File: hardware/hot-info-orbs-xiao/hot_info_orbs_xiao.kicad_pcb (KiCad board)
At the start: 2 copper layers, 198.8 x 28.5 mm, 13 parts, among them SW1 SW_Push, SW2 SW_Push, SW3 SW_Push, U2 XIAO ESP32-S3 Plus

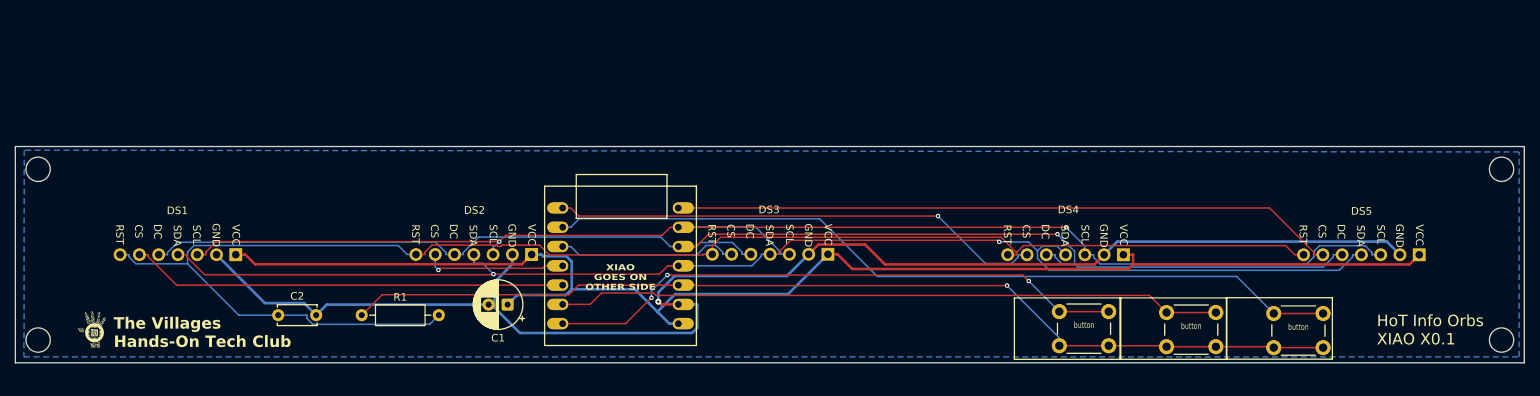
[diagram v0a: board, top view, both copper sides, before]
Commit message: xiao: physical rework, placed not routed (sockets, top-edge switches, no antenna patch)
Scott 2026-10-16: no antenna on the board, displays as low as possible on
headers into female sockets, right-angle 6x6x8 switches on the TOP edge
equally spaced in the centre third, C1/C2/R1 to the bottom. Physicals
first, route after he checks the STEP - so all tracks are stripped and the
pour is unfilled; DRC shows 46 unconnected and 0 parity on purpose.

- ANTENNA_PATCH and its silk removed; antenna_patch.py retired.
- DS1-5 -> new _Displays:GC9A01_SOCKET (same pads, PinSocket_1x07 model,
  display lifted 8.5 mm), pad row y 106.01 = the 0.5 mm edge rule + margin.
- SW1-3 -> stock PTS645Vx39 right-angle. Rejected the other PTS645 angled
  variants: Vx39's 8.05 mm overall depth is the one nearest "6x6x8". Its
  7.0 mm tab pitch vs the listing's 6.5 mm is unverified - measure a part.
- R1 in the DS1/DS2 gap, C1+C2 in DS3/DS4. Rejected the DS2/DS3 gap: the
  XIAO is on the back there and THT leads would hit it.
- Every Remove deferred to the end: after the first b.Remove() SWIG stops
  typing every return value, not just Zones() as HANDOFF had it.

Co-Authored-By: Claude Opus 5.5 <noreply@anthropic.com>
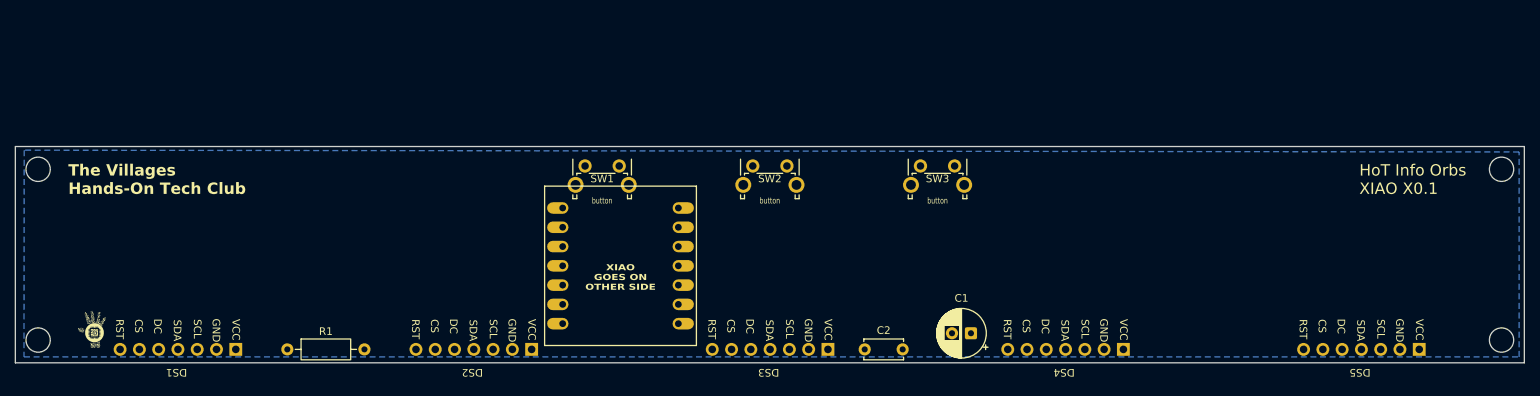
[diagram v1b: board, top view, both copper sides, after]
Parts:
- DS1, DS2, DS3, DS4, DS5: footprint _Displays:GC9A01_PINS -> _Displays:GC9A01_SOCKET
- SW1, SW2, SW3: footprint Button_Switch_THT:SW_PUSH_6mm_H5mm -> Button_Switch_THT:SW_Tactile_SPST_Angled_PTS645Vx39-2LFS
- moved C2 77.4 mm to (163.3, 106.0)
- moved SW1 65.4 mm to (126.4, 81.8)
- moved C1 61.2 mm to (177.3, 103.9)
- moved SW2 57.8 mm to (148.5, 81.8)
- moved SW3 50.4 mm to (170.6, 81.8)
- moved DS3 12.5 mm to (149.0, 102.5)
- moved DS2 12.5 mm to (110.0, 102.5)
- moved DS1 12.5 mm to (71.0, 102.5)
- moved DS4 12.5 mm to (188.0, 102.5)
- moved DS5 12.5 mm to (226.9, 102.5)
- moved R1 10.8 mm to (87.2, 106.0)
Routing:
- net /RST: track 202.3 -> 0.00 mm
- net GND: track 189.8 -> 0.00 mm, vias 1 -> 0
- net +5V: track 182.2 -> 0.00 mm
- net /SCLK: track 181.1 -> 0.00 mm, vias 2 -> 0
- net /DC: track 178.5 -> 0.00 mm, vias 1 -> 0
- net /MOSI: track 171.4 -> 0.00 mm, vias 2 -> 0
- net /3V3: track 132.3 -> 0.00 mm, vias 1 -> 0
- net /SW3: track 105.8 -> 0.00 mm
- net /SW2: track 87.8 -> 0.00 mm
- net /CS5: track 87.6 -> 0.00 mm
- net /SW1: track 77.1 -> 0.00 mm, vias 3 -> 0
- net /CS4: track 64.9 -> 0.00 mm, vias 1 -> 0
- net /CS1: track 57.6 -> 0.00 mm
- net /CS3: track 23.9 -> 0.00 mm
- net /CS2: track 18.8 -> 0.00 mm, vias 1 -> 0
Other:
- board text removed: "STICK FPC ANTENNA HERE no copper under this box"

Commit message: xiao: passives and switches to the XIAO's side, top edge up to the display tops
Scott 2026-10-16: "bottom of the board" meant the side, not the edge - C1,
C2, R1 and SW1-3 all go on the back with the XIAO. The switches stay on the
top edge. The top edge is raised to y 62.0, even with the display tops, so
the board is 45.78 mm tall. Still placed and not routed.

The display top was measured, not modeled. Rejected parsing the display
STEP's points, because the bounding box of an assembly STEP is meaningless.
It was measured from an orthographic render of the placed board against a
footprint-free copy at the same camera.

The top mounting holes moved up with the edge and keep their 3 mm corner
inset. The GND pour outline was rebuilt to the new edge.

The switch tabs no longer overlap the XIAO, since they now sit 17 mm
higher.

Flipped passives are re-centred on their pre-flip pad midpoint. Flip()
mirrors about pad 1, which put R1 into DS1's socket pads.

Co-Authored-By: Claude Opus 5.5 <noreply@anthropic.com>
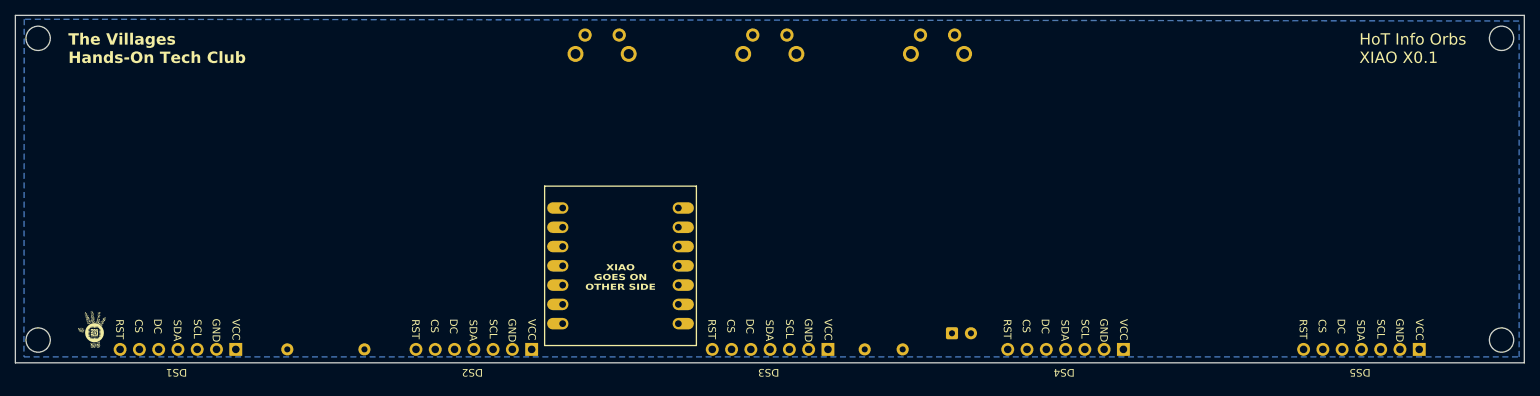
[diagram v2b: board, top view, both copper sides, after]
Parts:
- C1, C2, R1, SW1, SW2, SW3: moved to B.Cu
- moved SW1 17.8 mm to (130.9, 64.6), turned to 180 degrees
- moved SW2 17.8 mm to (153.0, 64.6), turned to 180 degrees
- moved SW3 17.8 mm to (175.1, 64.6), turned to 180 degrees
- moved R1 10.2 mm to (97.4, 106.0), turned to 180 degrees
- moved C2 5.00 mm to (168.3, 106.0), turned to 180 degrees
- moved C1 2.50 mm to (174.8, 103.9), turned to 0 degrees
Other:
- board size 198.8 x 28.5 mm -> 198.8 x 45.8 mm

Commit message: xiao: switches on the thirds, XIAO on sockets, board ID and HOT logo on the back
Scott 2026-10-16, third physical pass. The board is still placed and not
routed.

- Switches: one on the 1/3 line, one on the 2/3 line, one midway (x 117.63
  / 150.78 / 183.92). Pass 1 had centred them in three equal slots of the
  centre third, which was a misreading.
- XIAO uses the displays' arrangement: male headers into two 1x07 female
  sockets. The new XIAO-ESP32-S3-SOCKET footprint keeps Seeed's hole
  positions, which are already at the header holes; the DIP's drill offset
  moves only the copper. Drill is 1.0 mm with 1.7 mm pads, the same as the
  display sockets. The script asserts that every pad lands on the old hole.
- Board ID moved to the back, the XIAO's side. The 5 mm HOT logo becomes a
  28 mm copy built from the same polygons, scaled. A new bitmap trace was
  rejected because the vector art holds up when scaled. Font stays Comic
  Sans as on v1.1.
- Orphan "VCC"/"GND" back labels removed: they marked nothing even on
  1d4623f.

DRC: 0 parity, 46 unconnected (no tracks), 5 silk_edge warnings (socket
tab boxes).

Co-Authored-By: Claude Opus 5.5 <noreply@anthropic.com>
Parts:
- removed the G*** at (61.5, 103.4)
- added G***: LOGO, _Logos:Hot_Logo_28mm, B.Cu at (232.0, 83.0)
- U2: footprint _ESP32 modules:XIAO-ESP32-S3-DIP -> _ESP32 modules:XIAO-ESP32-S3-SOCKET
- moved SW3 11.0 mm to (186.2, 64.6)
- moved SW1 11.0 mm to (119.9, 64.6)
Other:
- board text added: "HoT Info Orbs"
- board text added: "XIAO ESP32-S3 · rev X0.1"
- board text removed: "GND"
- board text removed: "HoT Info Orbs XIAO X0.1"
- board text removed: "VCC"
